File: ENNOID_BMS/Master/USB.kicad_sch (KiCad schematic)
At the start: 12 parts, among them J14 SERIAL, Q26 BSS138, U7 CP2104

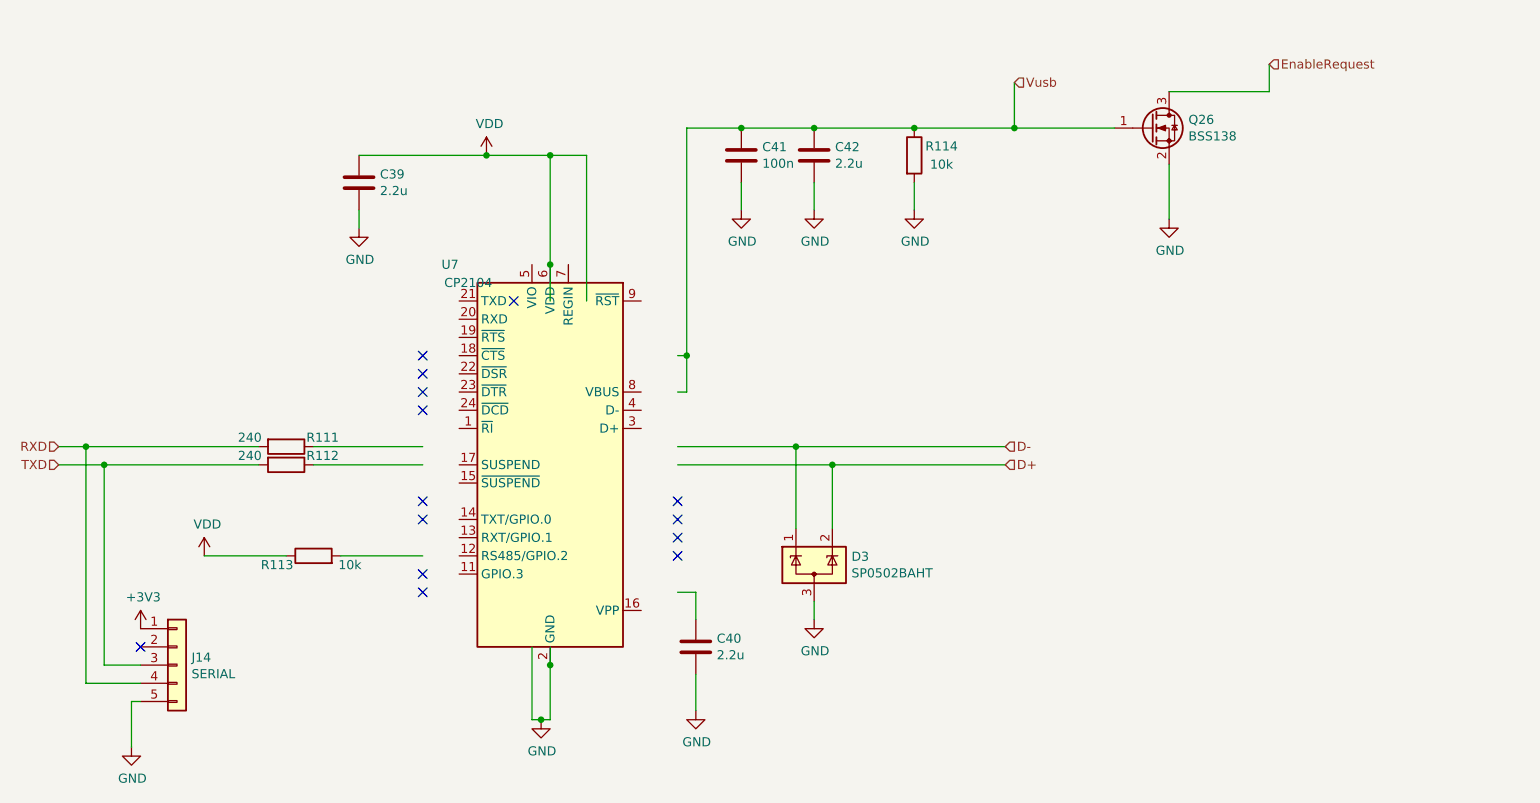
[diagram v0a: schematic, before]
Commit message: updated breakout
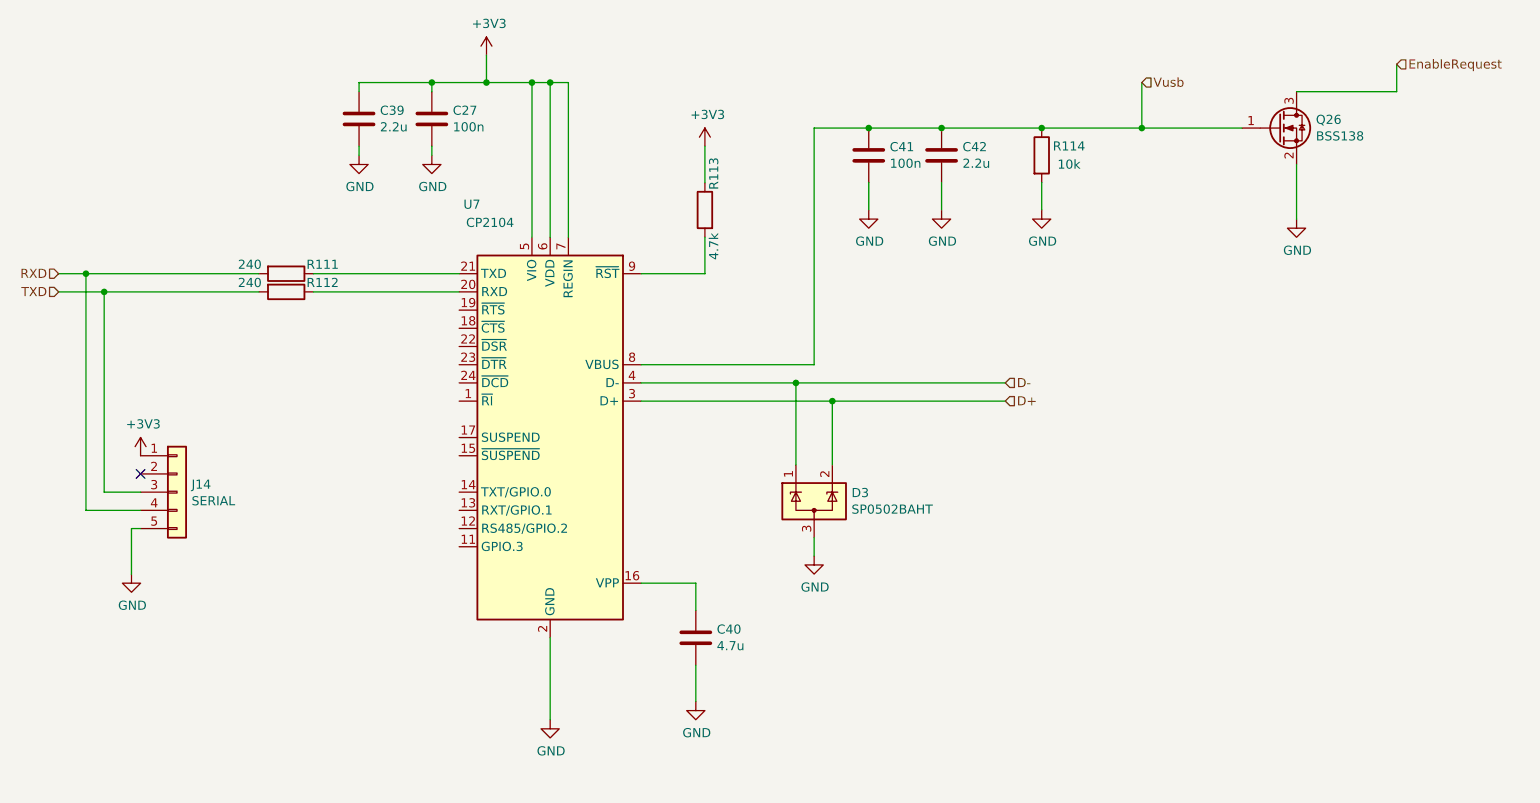
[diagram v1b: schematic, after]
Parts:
- added C27: 100n, Capacitor_SMD:C_0603_1608Metric, symbol BMS-Master-rescue:C-Device-BMS-Master-rescue
- C40: value 2.2u -> 4.7u; MPN GRM188R61A225KE34D -> (none)
- R113: value 10k -> 4.7k; MPN RC0603FR-0710KL -> (none)
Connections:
- net VDD is gone; now on net +3V3: C39.1, R113.1, U7.6 (VDD)
- net +3V3: now also U7.5 (VIO), U7.7 (REGIN), C27.1
- net D+: now also U7.3 (D+)
- net D-: now also U7.4 (D-)
- net GND: now also C27.2
- net Vusb: now also U7.8 (VBUS)
- net at U7.16 (VPP): now also C40.1
- net at U7.20 (RXD): now also R112.1
- net at U7.21 (TXD): now also R111.1
- net at U7.9 (~{RST}): now also R113.2
- no-connect marks 14 -> 1
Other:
- moved on the sheet: C39, C40, C41, C42, D3, J14, Q26, R111, R112, R113, R114, U7

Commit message: ENNOID BMS PCBs completed
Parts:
- D3, Q26: footprint TO_SOT_Packages_SMD:SOT-23 -> Package_TO_SOT_SMD:SOT-23
- J14: footprint Connectors_Molex:Molex_KK-6410-05_05x2.54mm_Straight -> Connector_Molex:Molex_KK-254_AE-6410-05A_1x05_P2.54mm_Vertical
- U7: footprint Housings_DFN_QFN:QFN-24-1EP_4x4mm_Pitch0.5mm -> Package_DFN_QFN:QFN-24-1EP_4x4mm_P0.5mm_EP2.7x2.7mm
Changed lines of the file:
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@@
 			)
 		)
-		(property "Footprint" "Housings_DFN_QFN:QFN-24-1EP_4x4mm_Pitch0.5mm"
+		(property "Footprint" "Package_DFN_QFN:QFN-24-1EP_4x4mm_P0.5mm_EP2.7x2.7mm"
 			(at 132.08 111.76 0)
 			(effects
@@
 			)
 		)
-		(property "Footprint" "TO_SOT_Packages_SMD:SOT-23"
+		(property "Footprint" "Package_TO_SOT_SMD:SOT-23"
 			(at 178.435 97.79 0)
 			(effects
@@
 			)
 		)
-		(property "Footprint" "TO_SOT_Packages_SMD:SOT-23"
+		(property "Footprint" "Package_TO_SOT_SMD:SOT-23"
 			(at 242.57 46.355 0)
 			(effects
@@
 			)
 		)
-		(property "Footprint" "Connectors_Molex:Molex_KK-6410-05_05x2.54mm_Straight"
+		(property "Footprint" "Connector_Molex:Molex_KK-254_AE-6410-05A_1x05_P2.54mm_Vertical"
 			(at 83.82 95.25 0)
 			(effects

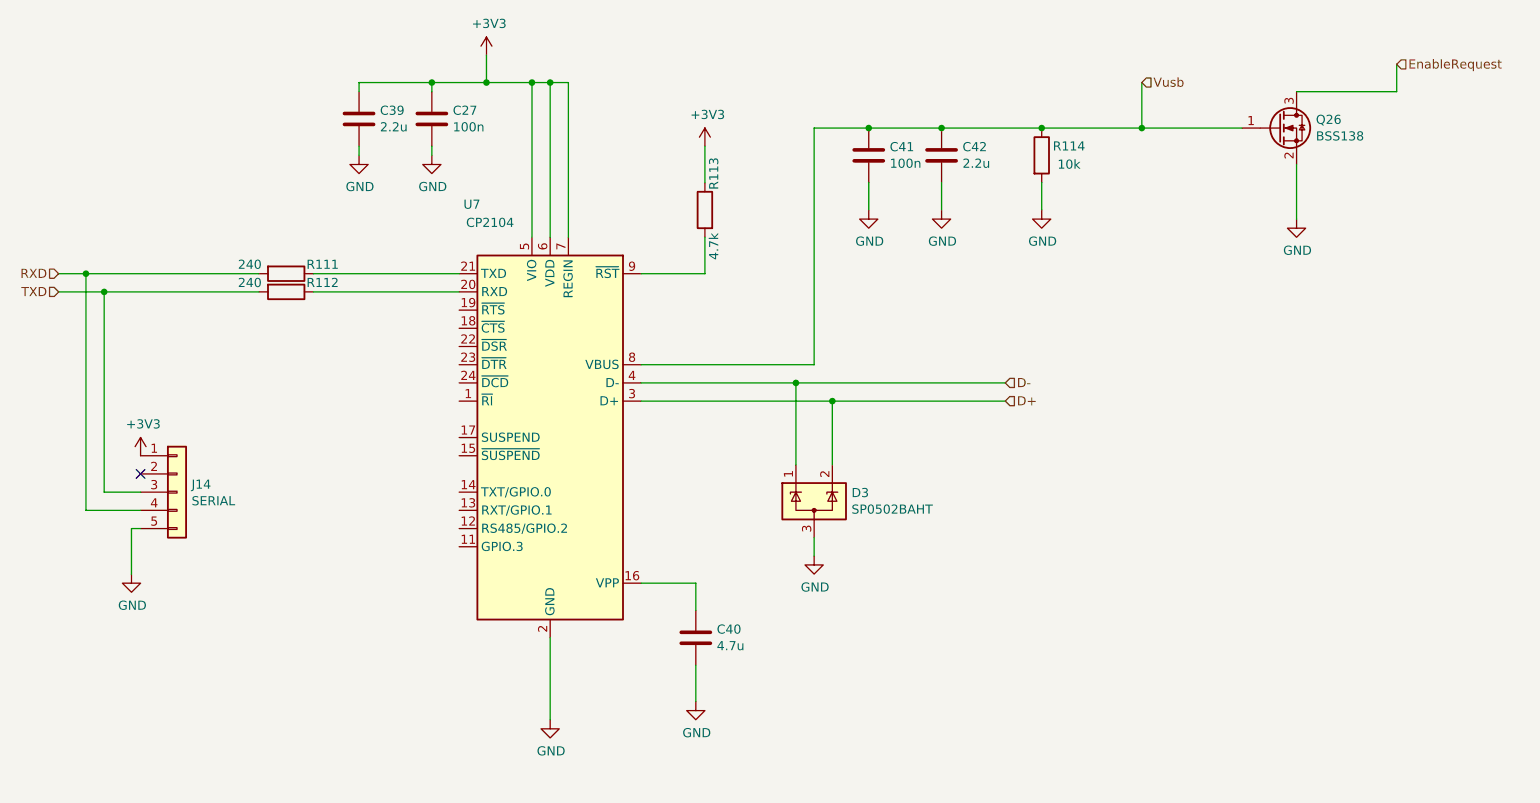
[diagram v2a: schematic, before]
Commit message: Slave with SMD and no other fuses
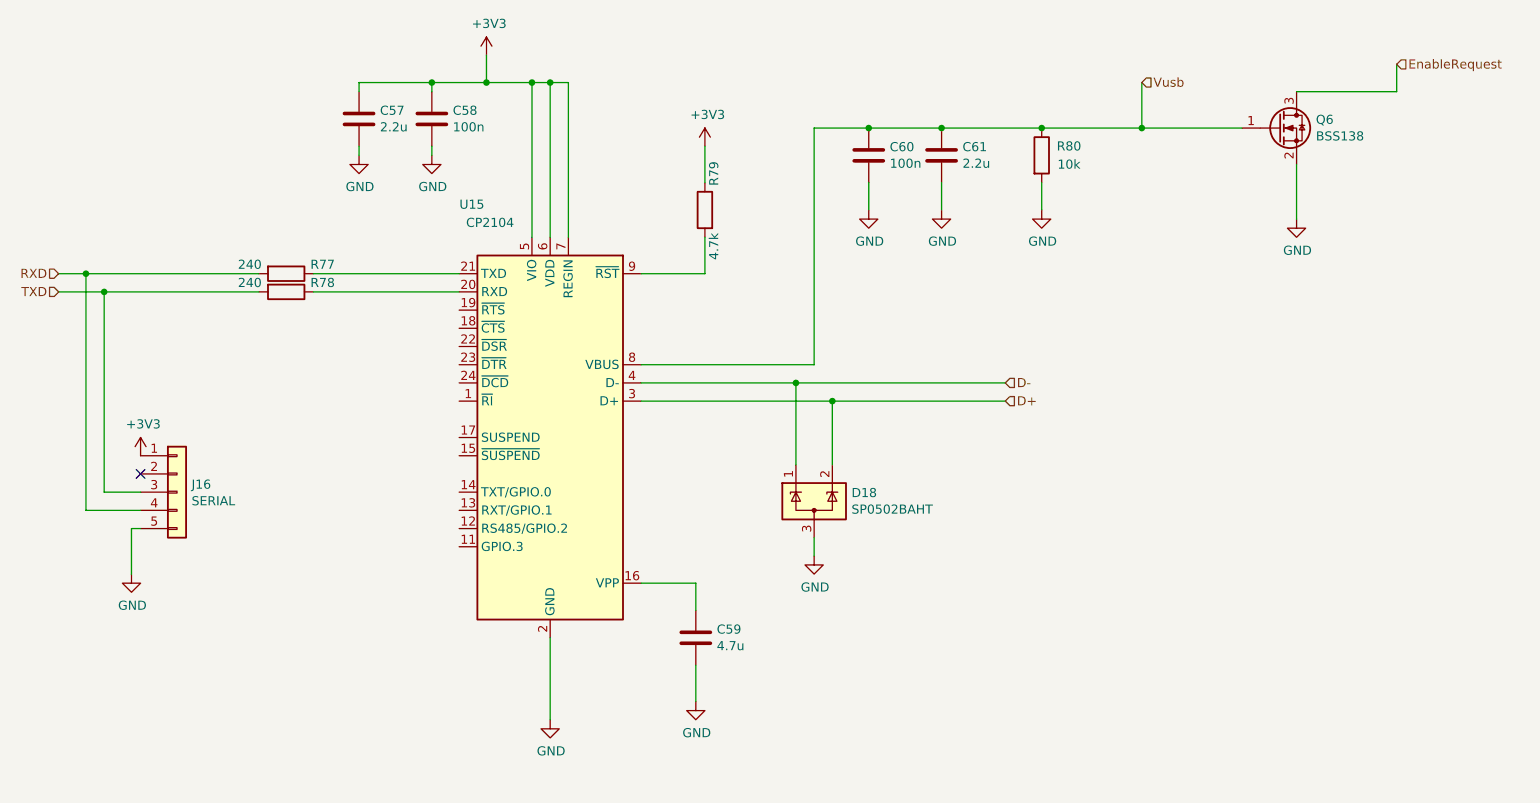
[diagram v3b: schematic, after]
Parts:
- C59: renamed from C40; MPN (none) -> GRM188Z71A475ME15D
- J16: renamed from J14; footprint Connector_Molex:Molex_KK-254_AE-6410-05A_1x05_P2.54mm_Vertical -> Connector_JST:JST_XH_B5B-XH-A_1x05_P2.50mm_Vertical; MPN 70543-0004 -> B5B-XH-A
- R79: renamed from R113; MPN (none) -> RC0603JR-074K7L
- renumbered C39 to C57, C27 to C58, C41 to C60, C42 to C61, D3 to D18, Q26 to Q6, R111 to R77, R112 to R78, R114 to R80, U7 to U15
